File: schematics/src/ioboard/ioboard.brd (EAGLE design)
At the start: 81.3 x 99.1 mm, 72 parts, among them IC1 TL072P, IC2 TL072P, IC3 TL072P

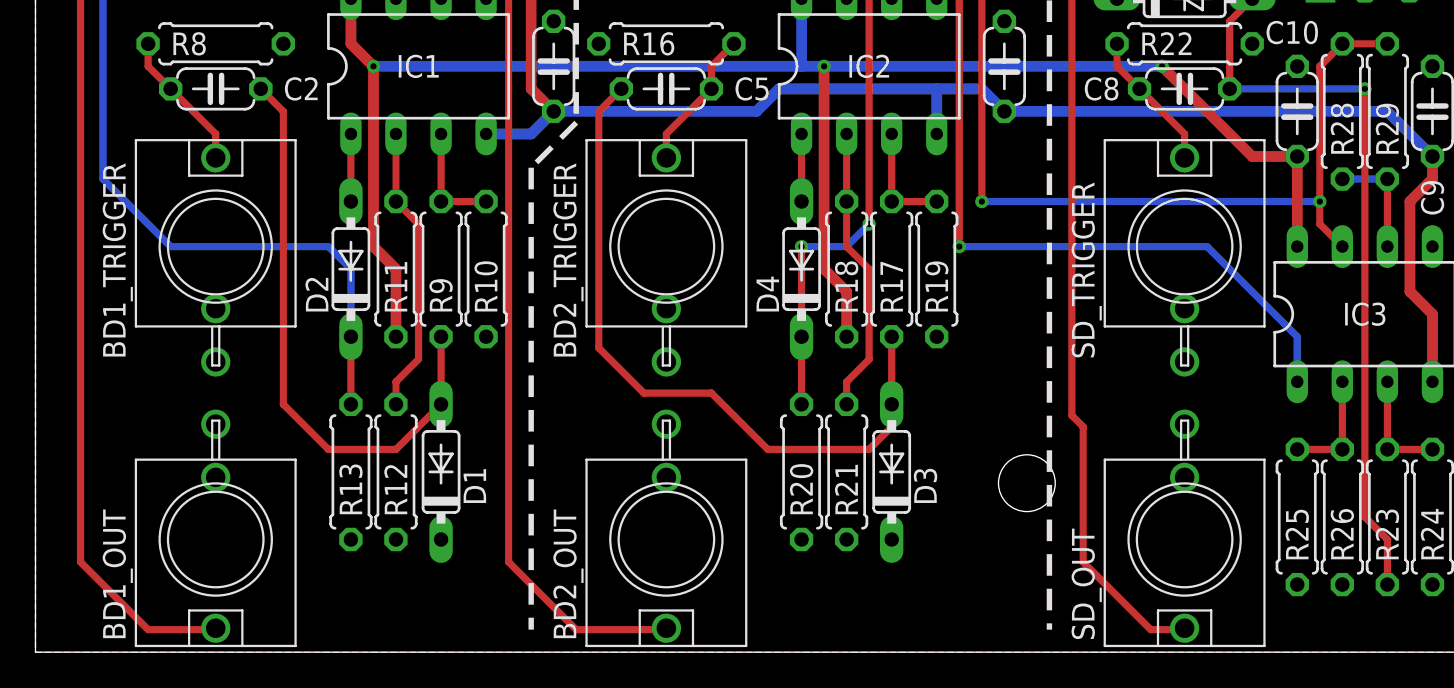
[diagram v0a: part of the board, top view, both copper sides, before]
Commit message: Updated Schematics, Fixed Power Socket orientation
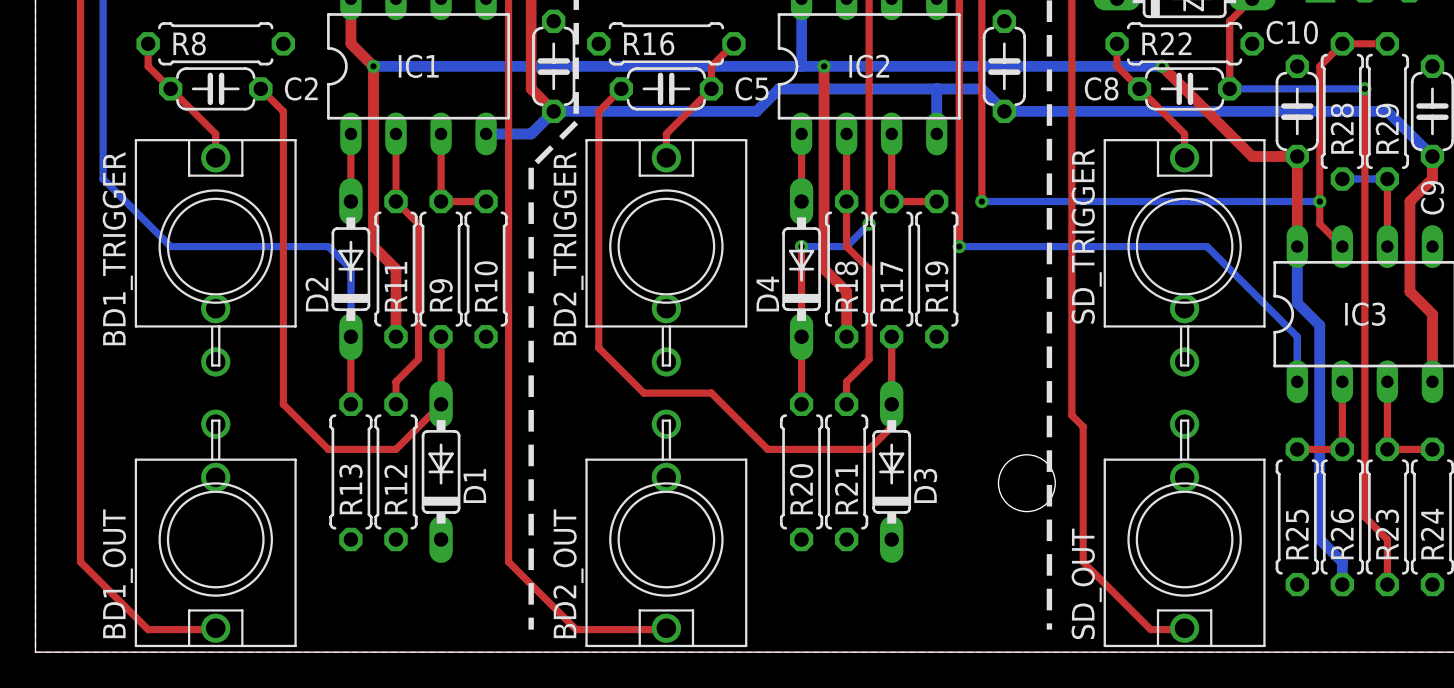
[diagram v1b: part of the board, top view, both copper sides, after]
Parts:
- BD1_TONE, BD1_TUNE, BD2_TUNE: value ALPHA-9MMA -> 50k log
- BD2_DECAY: value ALPHA-9MMA -> 1M log
- C1: value (none) -> 1uF/50v
- C16: value 1u/50v -> 1uF/50v
- C17: value 0.01u -> .01uF
- R2: value (none) -> 220
- R5: value (none) -> 4.7k
- SD_DECAY, SD_NOISE: value ALPHA-9MMA -> 100k lin
- SD_SNAPPY: value ALPHA-9MMA -> 50k lin
- SD_TUNE: value ALPHA-9MMA -> 1k lin
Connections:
- net +12V: now also R26.1
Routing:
- net +12V: track 150.3 -> 170.5 mm

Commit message: Some updates & bugfixes
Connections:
- new net N$26: IC3.7, R28.2, SD_VOLUME.3
- net SD_INT_OUT: no longer IC3.7, R28.2, SD_VOLUME.3
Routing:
- net N$26: track 0.00 -> 74.5 mm
- net SD_INT_OUT: track 178.2 -> 161.6 mm
- net SD_TUNE_A: track 35.5 -> 34.4 mm
- net N$5: track 93.7 -> 93.1 mm
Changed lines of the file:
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@@
 <wire x1="64.77" y1="1.27" x2="62.865" y2="1.27" width="0.4064" layer="1"/>
 <wire x1="62.865" y1="1.27" x2="59.055" y2="5.08" width="0.4064" layer="1"/>
-<wire x1="58.42" y1="57.15" x2="66.04" y2="64.77" width="0.4064" layer="1"/>
-<wire x1="66.04" y1="64.77" x2="66.04" y2="82.55" width="0.4064" layer="1"/>
-<wire x1="66.04" y1="82.55" x2="62.23" y2="86.36" width="0.4064" layer="1"/>
+<wire x1="58.42" y1="57.15" x2="65.405" y2="64.135" width="0.4064" layer="1"/>
+<wire x1="65.405" y1="64.135" x2="65.405" y2="83.185" width="0.4064" layer="1"/>
+<wire x1="65.405" y1="83.185" x2="62.23" y2="86.36" width="0.4064" layer="1"/>
 <wire x1="59.055" y1="5.08" x2="59.055" y2="12.7" width="0.4064" layer="1"/>
 <wire x1="59.055" y1="12.7" x2="58.42" y2="13.335" width="0.4064" layer="1"/>
@@
 </signal>
 <signal name="SD_INT_OUT">
-<contactref element="SD_VOLUME" pad="3"/>
-<contactref element="IC3" pad="7"/>
-<contactref element="R28" pad="2"/>
 <contactref element="R29" pad="1"/>
 <contactref element="OUT_CON" pad="2"/>
-<wire x1="76.2" y1="34.29" x2="73.66" y2="34.29" width="0.4064" layer="1"/>
-<wire x1="73.66" y1="22.86" x2="72.39" y2="24.13" width="0.4064" layer="1"/>
-<wire x1="72.39" y1="24.13" x2="72.39" y2="25.4" width="0.4064" layer="1"/>
-<wire x1="72.39" y1="25.4" x2="72.39" y2="33.02" width="0.4064" layer="1"/>
-<wire x1="72.39" y1="33.02" x2="73.66" y2="34.29" width="0.4064" layer="1"/>
+<wire x1="77.47" y1="33.02" x2="77.47" y2="25.4" width="0.4064" layer="1"/>
 <wire x1="2.54" y1="90.17" x2="5.08" y2="90.17" width="0.4064" layer="1"/>
 <wire x1="5.08" y1="90.17" x2="6.35" y2="91.44" width="0.4064" layer="1"/>
-<wire x1="6.35" y1="91.44" x2="55.88" y2="91.44" width="0.4064" layer="1"/>
-<wire x1="55.88" y1="91.44" x2="67.31" y2="91.44" width="0.4064" layer="1"/>
-<wire x1="67.31" y1="91.44" x2="68.58" y2="90.17" width="0.4064" layer="1"/>
-<wire x1="68.58" y1="90.17" x2="68.58" y2="89.52" width="0.4064" layer="1"/>
-<wire x1="68.58" y1="89.52" x2="68.54" y2="89.52" width="0.4064" layer="1"/>
-<via x="72.39" y="25.4" extent="1-16" drill="0.35"/>
-<wire x1="72.39" y1="25.4" x2="53.34" y2="25.4" width="0.4064" layer="16"/>
+<wire x1="6.35" y1="91.44" x2="52.07" y2="91.44" width="0.4064" layer="1"/>
+<wire x1="52.07" y1="91.44" x2="55.88" y2="87.63" width="0.4064" layer="1"/>
+<via x="77.47" y="25.4" extent="1-16" drill="0.35"/>
+<wire x1="77.47" y1="25.4" x2="53.34" y2="25.4" width="0.4064" layer="16"/>
 <via x="53.34" y="25.4" extent="1-16" drill="0.35"/>
 <wire x1="53.34" y1="25.4" x2="53.34" y2="50.8" width="0.4064" layer="1"/>
@@
 <wire x1="52.07" y1="69.85" x2="52.07" y2="72.39" width="0.4064" layer="1"/>
 <wire x1="52.07" y1="72.39" x2="55.88" y2="76.2" width="0.4064" layer="1"/>
-<wire x1="55.88" y1="76.2" x2="55.88" y2="91.44" width="0.4064" layer="1"/>
+<wire x1="55.88" y1="76.2" x2="55.88" y2="87.63" width="0.4064" layer="1"/>
+<wire x1="76.2" y1="34.29" x2="77.47" y2="33.02" width="0.4064" layer="1"/>
 </signal>
 <signal name="SD_TRIGGER">
@@
 <contactref element="SD_TUNE" pad="3"/>
 <contactref element="SD_CON" pad="2"/>
-<wire x1="78.74" y1="88.9" x2="73.66" y2="88.9" width="0.4064" layer="1"/>
-<wire x1="73.66" y1="88.9" x2="72.39" y2="87.63" width="0.4064" layer="1"/>
-<wire x1="72.39" y1="87.63" x2="72.39" y2="72.39" width="0.4064" layer="1"/>
+<wire x1="78.74" y1="88.9" x2="75.565" y2="88.9" width="0.4064" layer="1"/>
+<wire x1="75.565" y1="88.9" x2="73.66" y2="86.995" width="0.4064" layer="1"/>
+<wire x1="73.66" y1="86.995" x2="73.66" y2="80.645" width="0.4064" layer="1"/>
+<wire x1="73.66" y1="80.645" x2="72.39" y2="79.375" width="0.4064" layer="1"/>
+<wire x1="72.39" y1="79.375" x2="72.39" y2="72.39" width="0.4064" layer="1"/>
 <via x="72.39" y="72.39" extent="1-16" drill="0.35"/>
 <wire x1="59.65" y1="72.39" x2="59.65" y2="71.74" width="0.4064" layer="16"/>
@@
 <wire x1="54.65" y1="48.88" x2="57.15" y2="48.88" width="0.4064" layer="1"/>
 <wire x1="57.15" y1="48.88" x2="57.15" y2="58.42" width="0.4064" layer="1"/>
-<wire x1="57.15" y1="58.42" x2="64.77" y2="66.04" width="0.4064" layer="1"/>
-<wire x1="64.77" y1="66.04" x2="64.77" y2="81.28" width="0.4064" layer="1"/>
-<via x="64.77" y="81.28" extent="1-16" drill="0.35"/>
-<wire x1="64.77" y1="81.28" x2="78.74" y2="81.28" width="0.4064" layer="16"/>
+<wire x1="57.15" y1="58.42" x2="64.135" y2="65.405" width="0.4064" layer="1"/>
+<wire x1="64.135" y1="65.405" x2="64.135" y2="81.28" width="0.4064" layer="1"/>
+<via x="64.135" y="81.28" extent="1-16" drill="0.35"/>
+<wire x1="64.135" y1="81.28" x2="78.74" y2="81.28" width="0.4064" layer="16"/>
 </signal>
 <signal name="SD_SNAPPY_A">
 <contactref element="SD_SNAPPY" pad="3"/>
 <contactref element="SD_CON" pad="4"/>
-<wire x1="78.74" y1="83.82" x2="67.31" y2="83.82" width="0.4064" layer="16"/>
-<via x="67.31" y="83.82" extent="1-16" drill="0.35"/>
-<wire x1="67.31" y1="83.82" x2="67.31" y2="56.515" width="0.4064" layer="1"/>
+<wire x1="78.74" y1="83.82" x2="66.675" y2="83.82" width="0.4064" layer="16"/>
+<via x="66.675" y="83.82" extent="1-16" drill="0.35"/>
+<wire x1="66.675" y1="83.82" x2="66.675" y2="55.88" width="0.4064" layer="1"/>
 <wire x1="59.65" y1="48.895" x2="59.65" y2="48.88" width="0.4064" layer="1"/>
-<wire x1="67.31" y1="56.515" x2="59.65" y2="48.895" width="0.4064" layer="1"/>
+<wire x1="66.675" y1="55.88" x2="59.65" y2="48.895" width="0.4064" layer="1"/>
 </signal>
 <signal name="SD_NOISE_VOL_A">
@@
 <wire x1="54.61" y1="30.48" x2="76.2" y2="30.48" width="0.6096" layer="16"/>
 <wire x1="76.2" y1="30.48" x2="78.74" y2="27.94" width="0.6096" layer="16"/>
-<wire x1="78.74" y1="27.94" x2="78.74" y2="26.67" width="0.6096" layer="1"/>
-<wire x1="78.74" y1="26.67" x2="77.47" y2="25.4" width="0.6096" layer="1"/>
-<wire x1="77.47" y1="25.4" x2="77.47" y2="20.32" width="0.6096" layer="1"/>
+<wire x1="78.74" y1="27.94" x2="78.74" y2="25.4" width="0.6096" layer="1"/>
+<wire x1="78.74" y1="25.4" x2="77.47" y2="24.13" width="0.6096" layer="1"/>
+<wire x1="77.47" y1="24.13" x2="77.47" y2="20.32" width="0.6096" layer="1"/>
 <wire x1="77.47" y1="20.32" x2="78.74" y2="19.05" width="0.6096" layer="1"/>
 <wire x1="78.74" y1="19.05" x2="78.74" y2="15.24" width="0.6096" layer="1"/>
@@
 <wire x1="76.2" y1="26.67" x2="73.66" y2="26.67" width="0.4064" layer="16"/>
 </signal>
+<signal name="N$26">
+<contactref element="IC3" pad="7"/>
+<contactref element="SD_VOLUME" pad="3"/>
+<contactref element="R28" pad="2"/>
+<wire x1="71.755" y1="86.36" x2="70.485" y2="87.63" width="0.4064" layer="1"/>
+<wire x1="70.485" y1="87.63" x2="69.215" y2="87.63" width="0.4064" layer="1"/>
+<wire x1="69.215" y1="87.63" x2="68.525" y2="88.265" width="0.4064" layer="1"/>
+<wire x1="68.54" y1="89.52" x2="68.525" y2="88.265" width="0.4064" layer="1"/>
+<wire x1="71.755" y1="86.36" x2="71.755" y2="80.645" width="0.4064" layer="1"/>
+<wire x1="71.755" y1="80.645" x2="67.945" y2="76.835" width="0.4064" layer="1"/>
+<wire x1="67.945" y1="40.64" x2="70.485" y2="38.1" width="0.4064" layer="1"/>
+<wire x1="70.485" y1="38.1" x2="70.485" y2="36.195" width="0.4064" layer="1"/>
+<wire x1="70.485" y1="36.195" x2="71.755" y2="34.925" width="0.4064" layer="1"/>
+<wire x1="71.755" y1="34.925" x2="73.025" y2="34.925" width="0.4064" layer="1"/>
+<wire x1="73.025" y1="34.925" x2="73.66" y2="34.29" width="0.4064" layer="1"/>
+<wire x1="67.945" y1="76.835" x2="67.945" y2="40.64" width="0.4064" layer="1"/>
+<wire x1="73.66" y1="34.29" x2="73.66" y2="29.21" width="0.4064" layer="1"/>
+<wire x1="73.66" y1="29.21" x2="72.39" y2="27.94" width="0.4064" layer="1"/>
+<wire x1="72.39" y1="27.94" x2="72.39" y2="25.4" width="0.4064" layer="1"/>
+<wire x1="72.39" y1="25.4" x2="73.66" y2="24.13" width="0.4064" layer="1"/>
+<wire x1="73.66" y1="24.13" x2="73.66" y2="22.86" width="0.4064" layer="1"/>
+</signal>
 </signals>
